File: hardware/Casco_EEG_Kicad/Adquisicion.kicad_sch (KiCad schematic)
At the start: 46 parts, among them J1 Jack_Touch-Proof, J10 Jack_Touch-Proof, J11 Jack_Touch-Proof, J2 Jack_Touch-Proof, J3 Jack_Touch-Proof, J4 Jack_Touch-Proof, J5 Jack_Touch-Proof, J6 Jack_Touch-Proof, J7 Jack_Touch-Proof, J8 Jack_Touch-Proof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

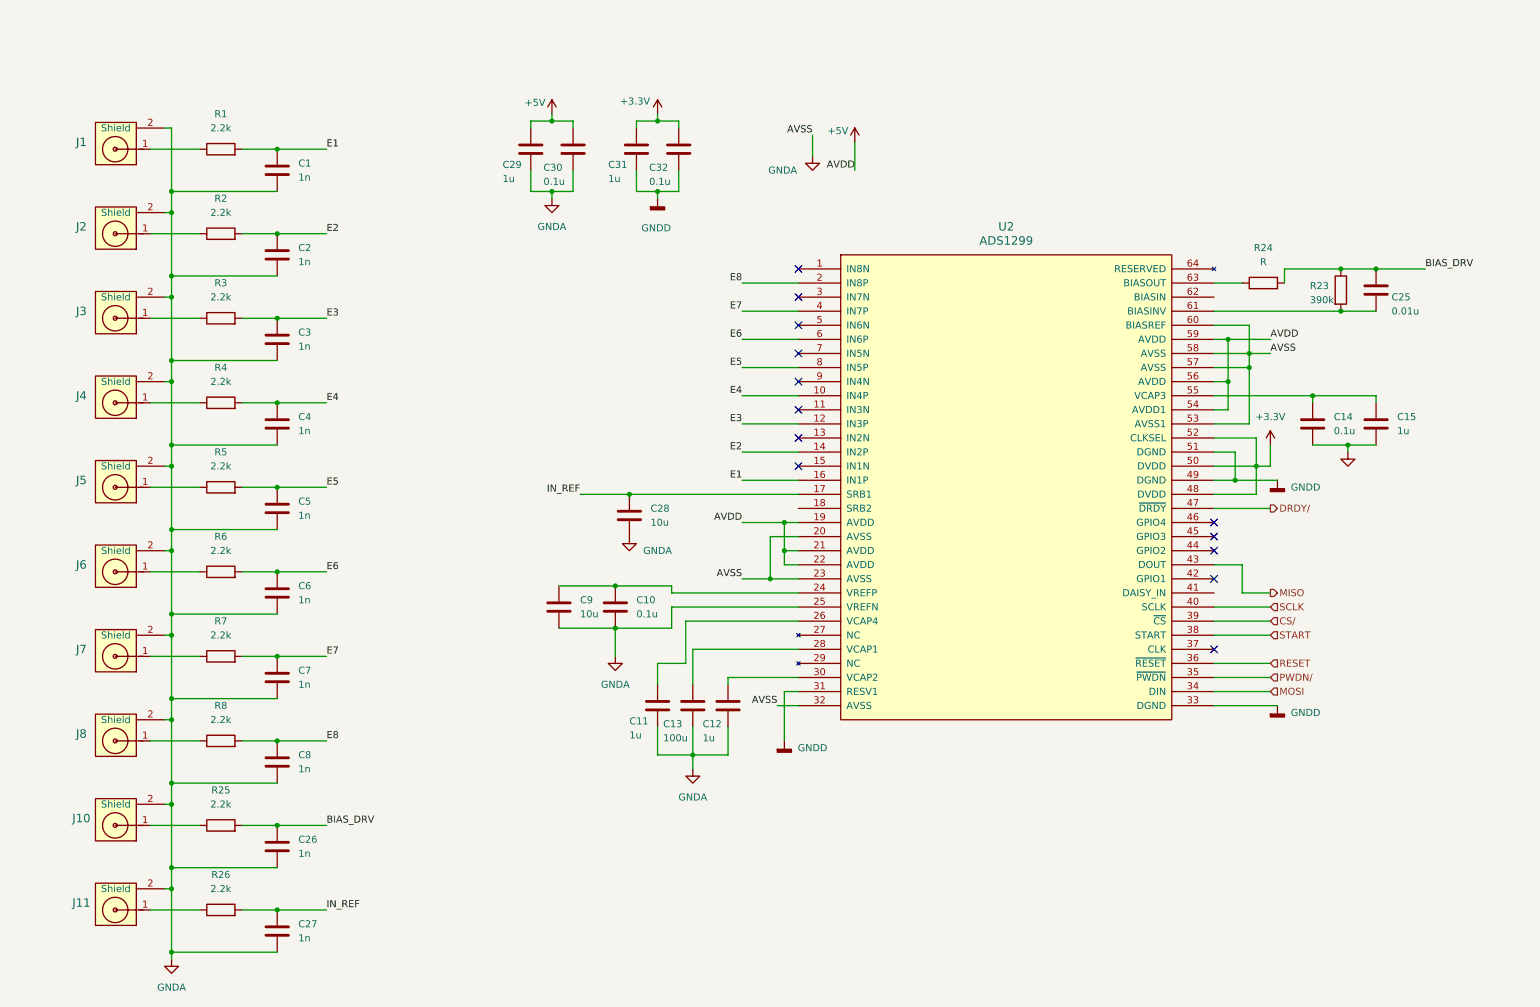
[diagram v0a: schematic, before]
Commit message: Primera implementacion de PCB, cambios varios
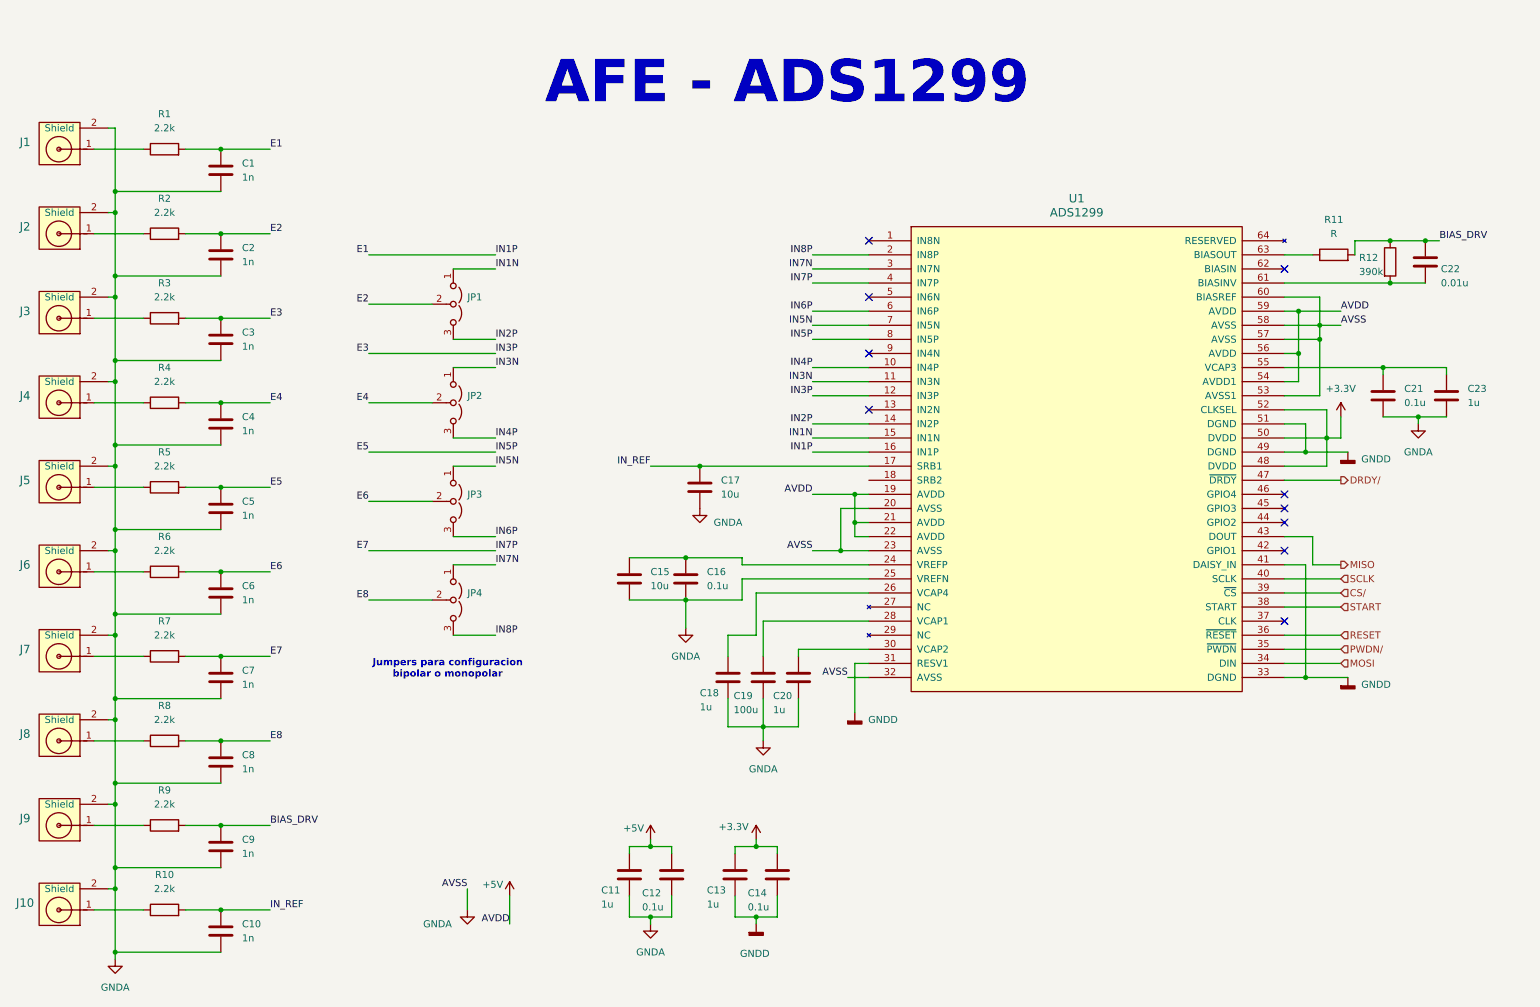
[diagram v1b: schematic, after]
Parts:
- added JP1, JP2, JP3, JP4: Jumper_3_Open, Connector_PinHeader_2.54mm:PinHeader_1x03_P2.54mm_Vertical, symbol Jumper:Jumper_3_Open
- C1, C2, C3, C4, C5, C6, C7, C8: footprint Capacitor_SMD:CP_Elec_3x5.4 -> Capacitor_SMD:C_0603_1608Metric
- C10: renamed from C27; footprint Capacitor_SMD:CP_Elec_3x5.4 -> Capacitor_SMD:C_0603_1608Metric
- C11: renamed from C29; footprint (none) -> Capacitor_SMD:C_0603_1608Metric
- C12: renamed from C30; footprint (none) -> Capacitor_SMD:C_0603_1608Metric
- C13: renamed from C31; footprint (none) -> Capacitor_SMD:C_0603_1608Metric
- C14: renamed from C32; footprint (none) -> Capacitor_SMD:C_0603_1608Metric
- C15: renamed from C9; footprint (none) -> Capacitor_SMD:C_0603_1608Metric
- C16: renamed from C10; footprint (none) -> Capacitor_SMD:C_0603_1608Metric
- C17: renamed from C28; footprint (none) -> Capacitor_SMD:C_0603_1608Metric
- C18: renamed from C11; footprint (none) -> Capacitor_SMD:C_0603_1608Metric
- C19: renamed from C13; footprint (none) -> Capacitor_SMD:C_0603_1608Metric
- C20: renamed from C12; footprint (none) -> Capacitor_SMD:C_0603_1608Metric
- C21: renamed from C14; footprint (none) -> Capacitor_SMD:C_0603_1608Metric
- C22: renamed from C25; footprint (none) -> Capacitor_SMD:C_0603_1608Metric
- C23: renamed from C15; footprint (none) -> Capacitor_SMD:C_0603_1608Metric
- C9: renamed from C26; footprint Capacitor_SMD:CP_Elec_3x5.4 -> Capacitor_SMD:C_0603_1608Metric
- R1, R2, R3, R4, R5, R6, R7, R8: footprint Resistor_SMD:R_0201_0603Metric -> Resistor_SMD:R_0603_1608Metric
- R10: renamed from R26; footprint Resistor_SMD:R_0201_0603Metric -> Resistor_SMD:R_0603_1608Metric
- R11: renamed from R24; footprint (none) -> Resistor_SMD:R_0603_1608Metric
- R12: renamed from R23; footprint (none) -> Resistor_SMD:R_0603_1608Metric
- R9: renamed from R25; footprint Resistor_SMD:R_0201_0603Metric -> Resistor_SMD:R_0603_1608Metric
- renumbered J11 to J10, J10 to J9, U2 to U1
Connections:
- net GND is gone; now on net GNDA: C21.2, C23.2
- net E2: now also JP1.2 (C); no longer U1.14 (IN2P)
- net E4: now also JP2.2 (C); no longer U1.10 (IN4P)
- net E6: now also JP3.2 (C); no longer U1.6 (IN6P)
- net E8: now also JP4.2 (C); no longer U1.2 (IN8P)
- net GNDD: now also U1.41 (DAISY_IN)
- net IN3N: now reaches U1.11 (IN3N)
- net IN3N: now also JP2.1 (A)
- net IN1N: now reaches U1.15 (IN1N)
- net IN1N: now also JP1.1 (A)
- net IN7N: now reaches U1.3 (IN7N)
- net IN7N: now also JP4.1 (A)
- net IN5N: now reaches U1.7 (IN5N)
- net IN5N: now also JP3.1 (A)
- new net IN2P: JP1.3 (B), U1.14 (IN2P)
- new net IN4P: JP2.3 (B), U1.10 (IN4P)
- new net IN6P: JP3.3 (B), U1.6 (IN6P)
- new net IN8P: JP4.3 (B), U1.2 (IN8P)
- no-connect marks 13 -> 10
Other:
- note added: "AFE - ADS1299"
- note added: "Jumpers para configuracion bipolar o monopolar"
- moved on the sheet: C1, C10, C11, C12, C13, C14, C15, C16, C17, C18, C19, C2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

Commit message: Nuevos cambios al PCB, mejoro planos, regulo 3,3V desde 5V, etc
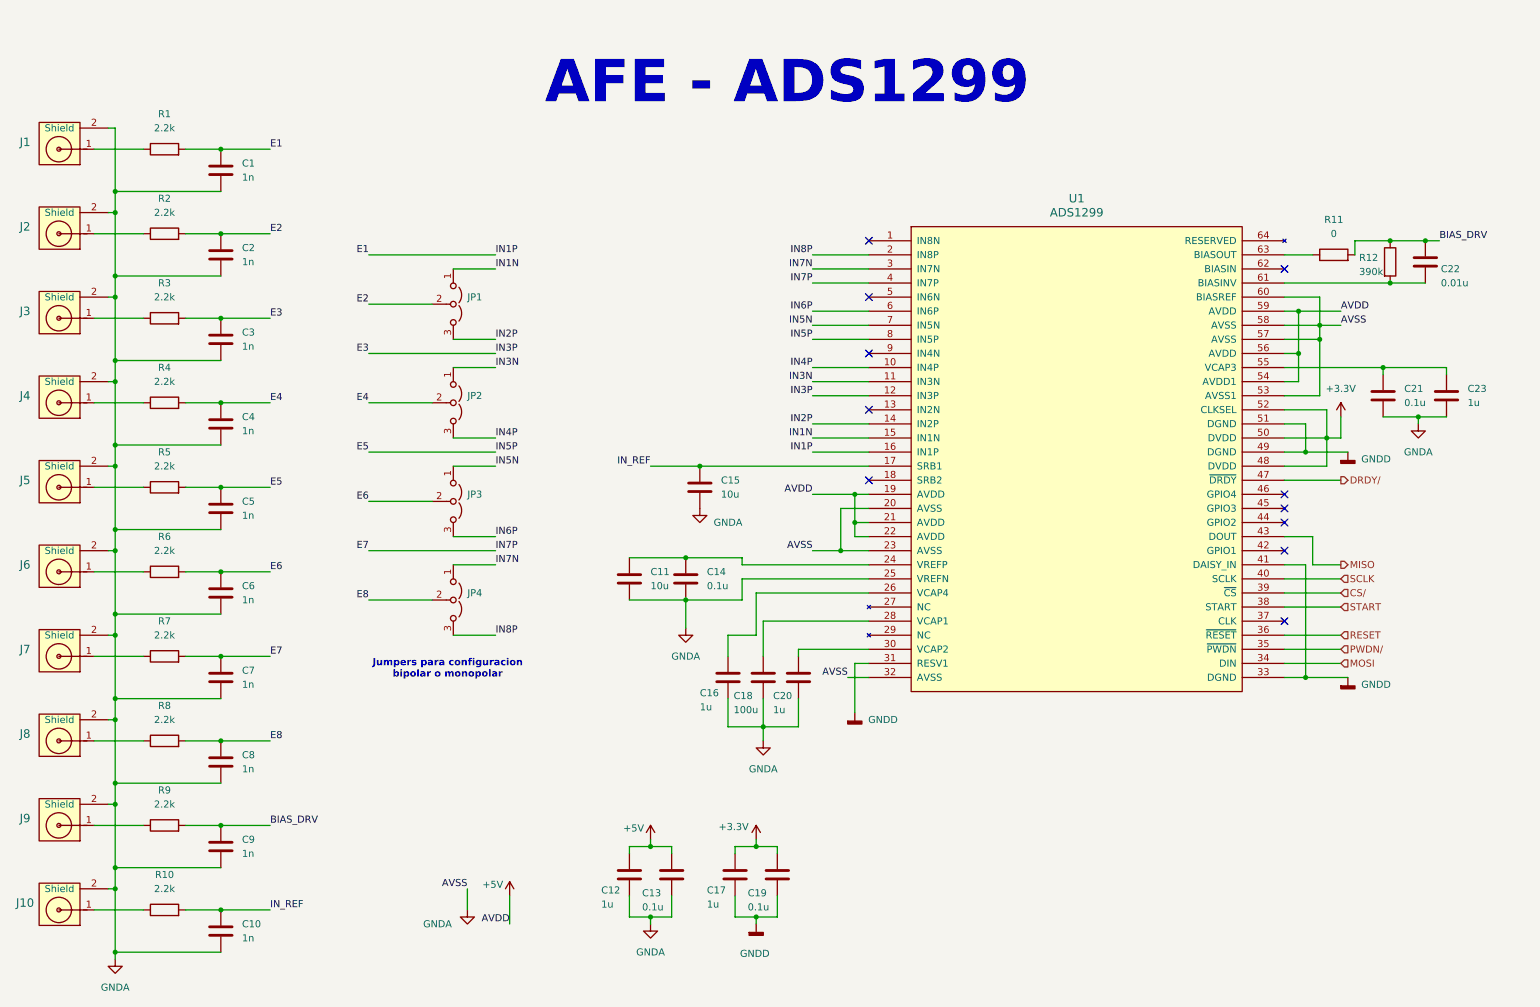
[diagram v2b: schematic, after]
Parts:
- C1, C10, C2, C3, C4, C5, C6, C7, C8, C9: LCSC PN (none) -> C1588
- C11: renamed from C15; LCSC PN (none) -> C19702
- C12: renamed from C11; LCSC PN (none) -> C15849
- C13: renamed from C12; LCSC PN (none) -> C48579280
- C14: renamed from C16; LCSC PN (none) -> C48579280
- C15: renamed from C17; LCSC PN (none) -> C19702
- C16: renamed from C18; LCSC PN (none) -> C15849
- C17: renamed from C13; LCSC PN (none) -> C15849
- C18: renamed from C19; footprint Capacitor_SMD:C_0603_1608Metric -> Capacitor_SMD:C_0805_2012Metric; LCSC PN (none) -> C141660
- C19: renamed from C14; LCSC PN (none) -> C48579280
- C20, C23: LCSC PN (none) -> C15849
- C21: LCSC PN (none) -> C48579280
- C22: LCSC PN (none) -> C57112
- R1, R10, R2, R3, R4, R5, R6, R7, R8, R9: LCSC PN (none) -> C114662
- R11: value R -> 0
- R12: LCSC PN (none) -> C23150
- U1: LCSC PN (none) -> C476817
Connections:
- no-connect marks 10 -> 11

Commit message: Implemento pines I/O para trigger
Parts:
- C13, C14, C19, C21: LCSC PN C48579280 -> C14663
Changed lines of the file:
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@@
 			)
 		)
-		(property "LCSC PN" "C48579280"
+		(property "LCSC PN" "C14663"
 			(at 264.16 81.28 0)
 			(effects
@@
 			)
 		)
-		(property "LCSC PN" "C48579280"
+		(property "LCSC PN" "C14663"
 			(at 138.43 114.3 0)
 			(effects
@@
 			)
 		)
-		(property "LCSC PN" "C48579280"
+		(property "LCSC PN" "C14663"
 			(at 154.94 167.64 0)
 			(effects
@@
 			)
 		)
-		(property "LCSC PN" "C48579280"
+		(property "LCSC PN" "C14663"
 			(at 135.89 167.64 0)
 			(effects

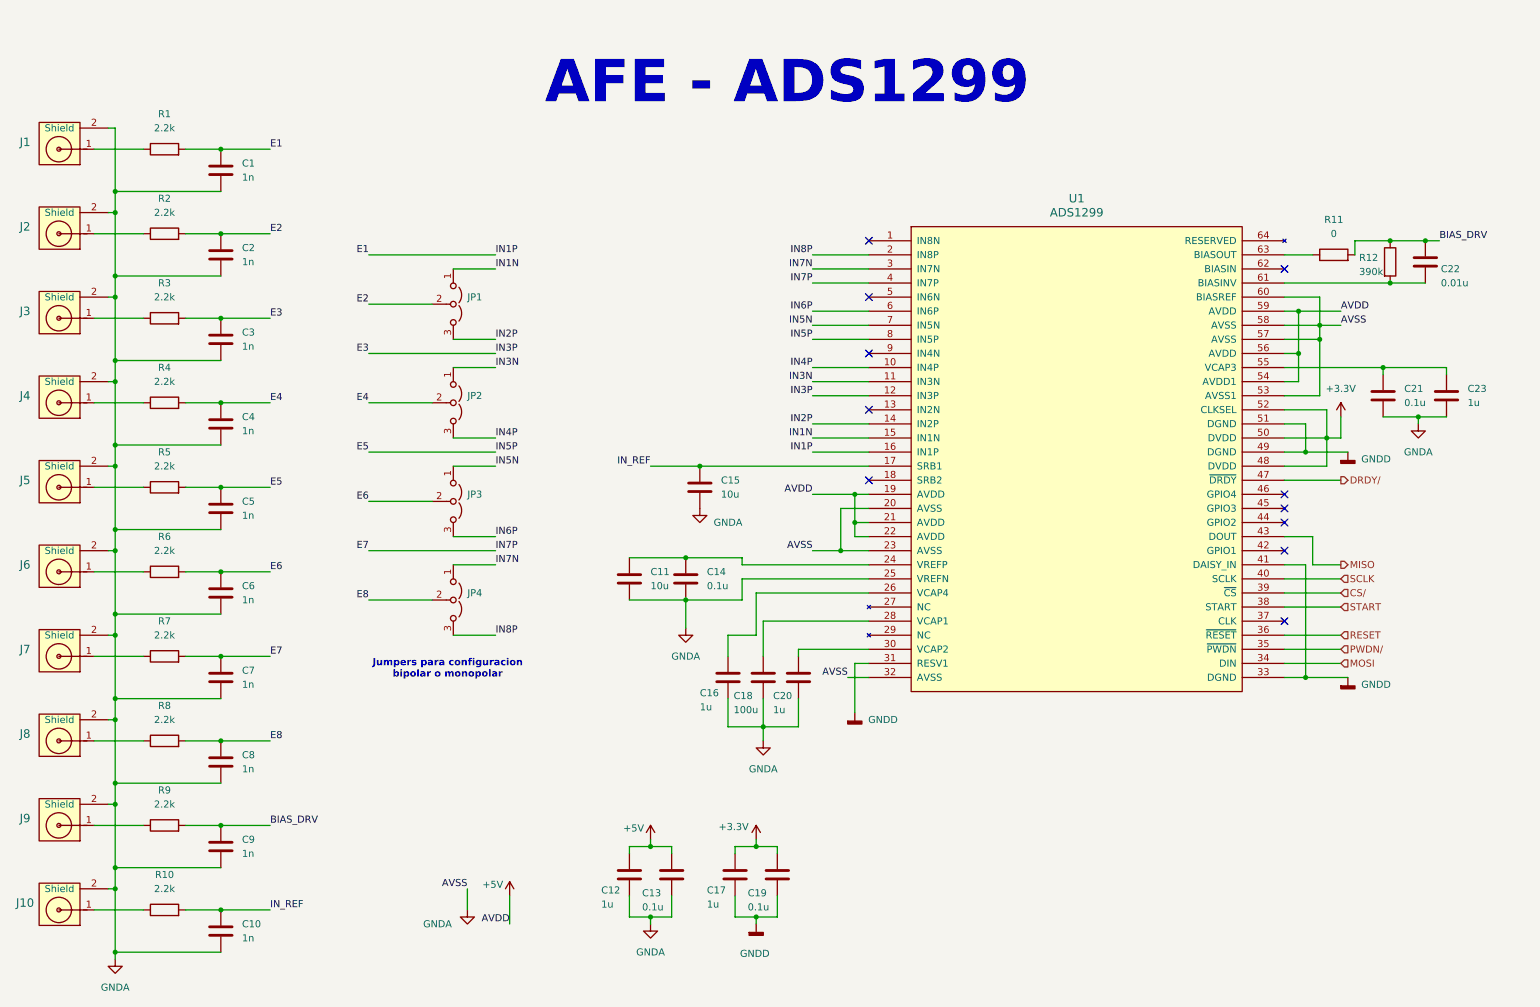
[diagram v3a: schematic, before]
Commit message: Agrego protecciones a las entradas analogicas, quito jumpers dealimentacion, agrego capacitores al HC05
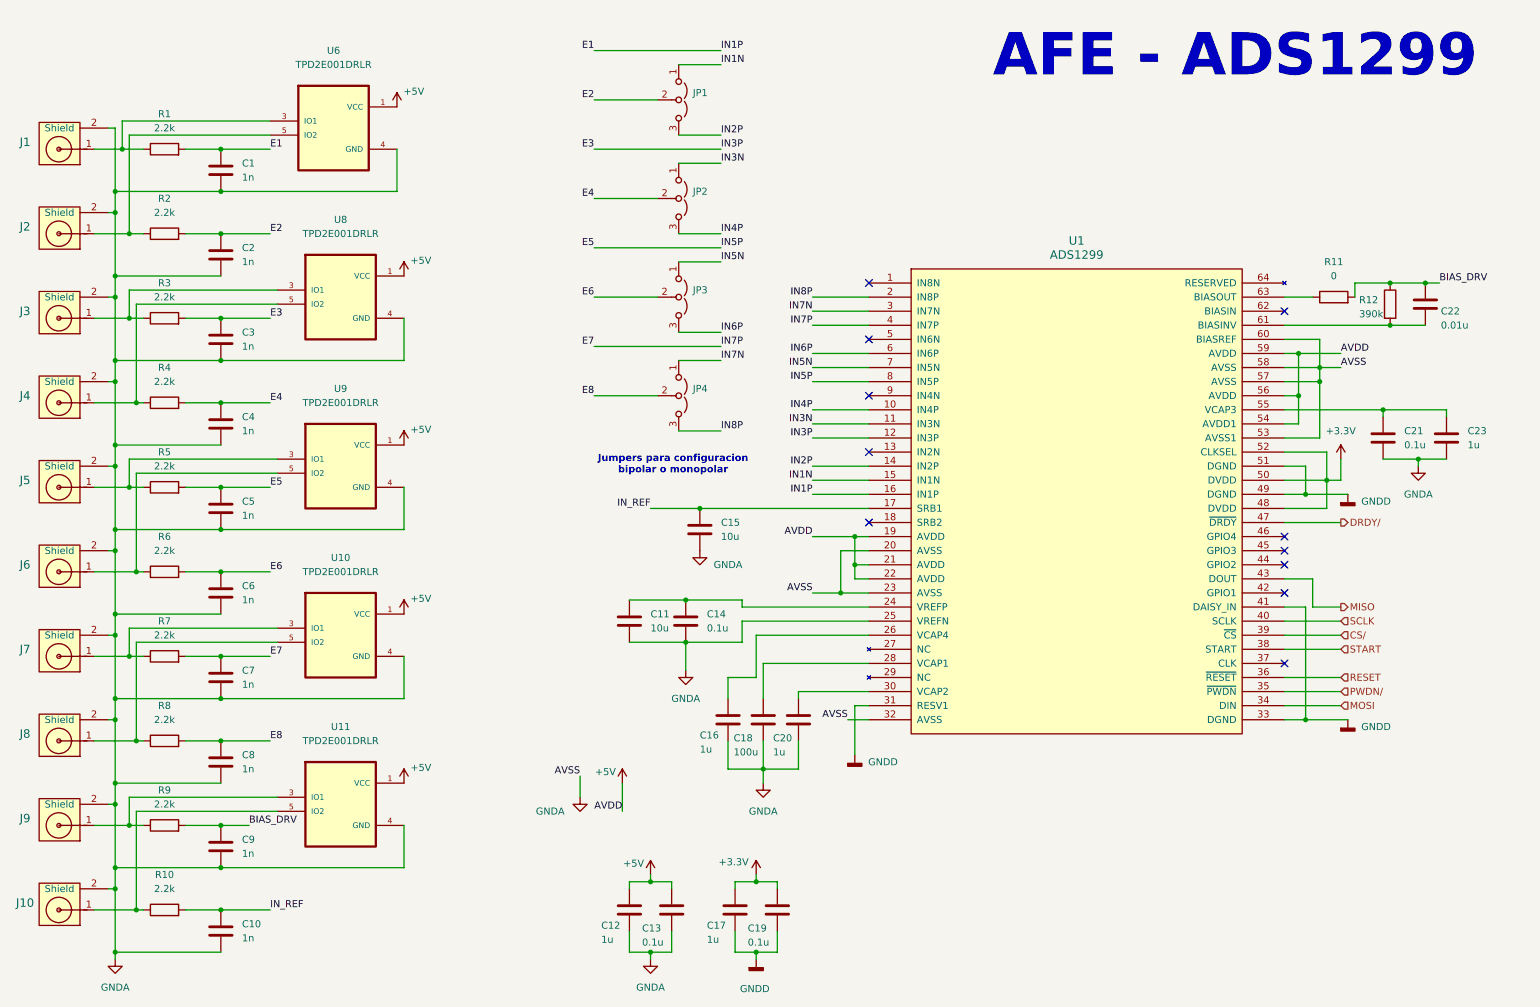
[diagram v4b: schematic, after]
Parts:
- added U10, U11, U6, U8, U9: TPD2E001DRLR, Huellas:SOT50P160X60-5N, symbol TPD2E001:TPD2E001DRLR
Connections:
- net +5V: now also U10.1 (VCC), U11.1 (VCC), U6.1 (VCC), U8.1 (VCC), U9.1 (VCC)
- net GNDA: now also U10.4 (GND), U11.4 (GND), U6.4 (GND), U8.4 (GND), U9.4 (GND)
- net at J4.1, R4.1: now also U8.5 (IO2)
- net at J6.1, R6.1: now also U9.5 (IO2)
- net at J10.1, R10.1: now also U11.5 (IO2)
- net at J8.1, R8.1: now also U10.5 (IO2)
- net at J1.1, R1.1: now also U6.3 (IO1)
- net at J3.1, R3.1: now also U8.3 (IO1)
- net at J9.1, R9.1: now also U11.3 (IO1)
- net at J5.1, R5.1: now also U9.3 (IO1)
- net at J2.1, R2.1: now also U6.5 (IO2)
- net at J7.1, R7.1: now also U10.3 (IO1)
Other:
- moved on the sheet: C11, C12, C13, C14, C15, C16, C17, C18, C19, C20, C21, C22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
